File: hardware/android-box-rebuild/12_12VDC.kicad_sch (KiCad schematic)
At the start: 30 parts, among them CN4 0533980271, Q1 YJL2305A, U1 100uF, U2 100uF, U3 TPS54531DDAR

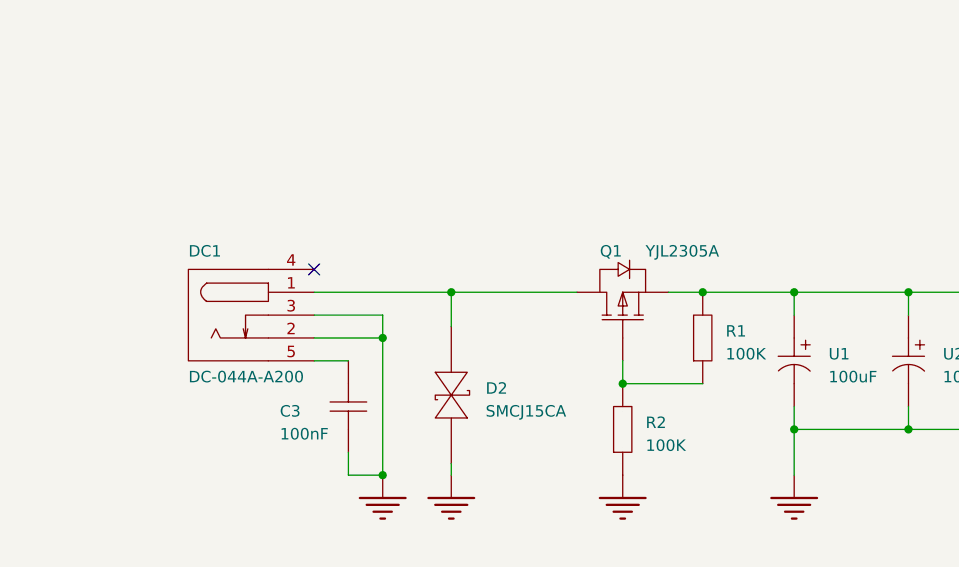
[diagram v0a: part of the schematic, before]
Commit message: Route J5 USB-C PD power front end
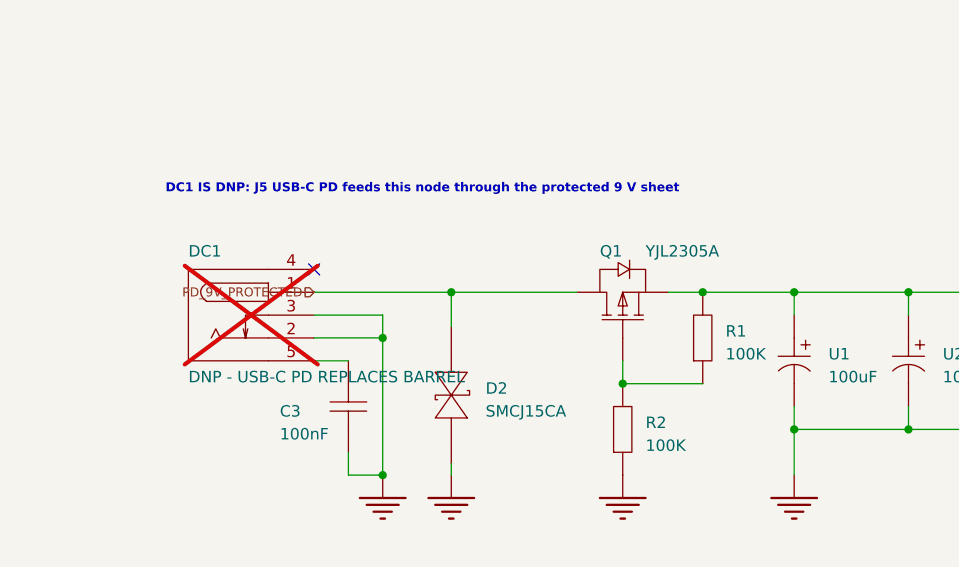
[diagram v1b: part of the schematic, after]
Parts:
- DC1: value DC-044A-A200 -> DNP - USB-C PD REPLACES BARREL; now not fitted; now left out of the parts list
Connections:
- net PD_9V_PROTECTED: now reaches D2.2, DC1.1, Q1.3 (D)
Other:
- note added: "DC1 IS DNP: J5 USB-C PD feeds this node through the protected 9 V sheet"
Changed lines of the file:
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@@
+		)
+	)
+	(hierarchical_label "PD_9V_PROTECTED"
+		(shape input)
+		(at 59.69 57.15 180)
+		(effects
+			(font
+				(size 1 1)
+			)
+			(justify right)
+		)
+	)
+	(text "DC1 IS DNP: J5 USB-C PD feeds this node through the protected 9 V sheet"
+		(exclude_from_sim no)
+		(at 43.18 45.72 0)
+		(effects
+			(font
+				(size 1 1)
+				(bold yes)
+			)
+			(justify left)
 		)
 	)
@@
 		(body_style 0)
 		(exclude_from_sim no)
-		(in_bom yes)
-		(on_board yes)
-		(in_pos_files yes)
-		(dnp no)
+		(in_bom no)
+		(on_board no)
+		(in_pos_files no)
+		(dnp yes)
 		(property "Reference" "DC1"
 			(at 45.72 53.34 0)
@@
 			)
 		)
-		(property "Value" "DC-044A-A200"
+		(property "Value" "DNP - USB-C PD REPLACES BARREL"
 			(at 45.72 67.31 0)
 			(show_name no)
